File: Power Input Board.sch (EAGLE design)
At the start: 14 parts, among them Q1 SPB80P06P

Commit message: reconstructing
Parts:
- added J1, J2: (no value), SparkFun-Connectors:BANANA_CONN
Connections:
- net N$12 renamed +48V_GND
- removed net N$9: U$5.48V_GND
- removed net VCC: Q1.G
- new net +48V_RAW: J1.1, Q1.G
- new net 48V_GND: J2.1, R3.1, U$5.48V_GND
- net 3.3V: no longer R3.1
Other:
- note added: "48 VOLT CONNECTOR"
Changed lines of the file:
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@@
 <setting verticaltext="up"/>
 </settings>
-<grid distance="1" unitdist="mm" unit="mm" style="lines" multiple="1" display="no" altdistance="0.01" altunitdist="inch" altunit="inch"/>
+<grid distance="0.1" unitdist="inch" unit="inch" style="lines" multiple="1" display="no" altdistance="0.01" altunitdist="inch" altunit="inch"/>
 <layers>
 <layer number="1" name="Top" color="4" fill="1" visible="no" active="no"/>
@@
 <attribute name="SPICEPREFIX" value="R"/>
 </part>
-<part name="GND2" library="SparkFun-PowerSymbols" library_urn="urn:adsk.eagle:library:530" deviceset="GND2" device=""/>
-<part name="+48V" library="audio amplifier example" library_urn="urn:adsk.eagle:library:970892" deviceset="VCC" device="" value="48V"/>
 <part name="Q1" library="transistor-fet" library_urn="urn:adsk.eagle:library:396" deviceset="SPB80P06P" device="" package3d_urn="urn:adsk.eagle:package:28539/2"/>
 <part name="U$2" library="board_outlines" deviceset="BOARD" device="PDB"/>
@@
 <part name="U$5" library="PDB_TO_BRICKS" deviceset="BRICK_TO_POWER_DIST_WHOLE" device=""/>
 <part name="U$6" library="PDB_TO_BRICKS" deviceset="BRICK_TO_POWER_DIST_WHOLE" device=""/>
+<part name="J1" library="SparkFun-Connectors" deviceset="BANANA_CONN" device=""/>
+<part name="J2" library="SparkFun-Connectors" deviceset="BANANA_CONN" device=""/>
 </parts>
 <sheets>
 <sheet>
 <plain>
+<text x="30.48" y="106.68" size="2.54" layer="91">48 VOLT CONNECTOR</text>
 </plain>
 <instances>
@@
 <attribute name="NAME" x="145.796" y="195.58" size="1.778" layer="95" font="vector" rot="R90" align="bottom-center"/>
 <attribute name="VALUE" x="148.844" y="195.58" size="1.778" layer="96" font="vector" rot="R90" align="top-center"/>
-</instance>
-<instance part="GND2" gate="G$1" x="147.32" y="182.88">
-<attribute name="VALUE" x="147.32" y="181.102" size="1.778" layer="96" align="top-center"/>
-</instance>
-<instance part="+48V" gate="VCC" x="142.24" y="223.52">
-<attribute name="VALUE" x="140.716" y="224.536" size="1.27" layer="96"/>
 </instance>
 <instance part="Q1" gate="G$1" x="144.78" y="213.36">
@@
 <instance part="U$5" gate="G$1" x="297.18" y="147.32"/>
 <instance part="U$6" gate="G$1" x="297.18" y="119.38"/>
+<instance part="J1" gate="G$1" x="50.8" y="96.52"/>
+<instance part="J2" gate="G$1" x="50.8" y="91.44"/>
 </instances>
 <busses>
@@
 <wire x1="73.66" y1="180.34" x2="58.42" y2="180.34" width="0.1524" layer="91"/>
 </segment>
-<segment>
-<pinref part="GND2" gate="G$1" pin="3.3V"/>
-<wire x1="147.32" y1="185.42" x2="147.32" y2="190.5" width="0.1524" layer="91"/>
-<pinref part="R3" gate="G$1" pin="1"/>
-</segment>
 </net>
 <net name="N$3" class="0">
@@
 </segment>
 </net>
-<net name="VCC" class="0">
-<segment>
-<pinref part="Q1" gate="G$1" pin="G"/>
-<pinref part="+48V" gate="VCC" pin="VCC"/>
-<wire x1="142.24" y1="215.9" x2="142.24" y2="220.98" width="0.1524" layer="91"/>
-</segment>
-</net>
 <net name="+12V_1" class="0">
 <segment>
@@
 </segment>
 </net>
-<net name="N$9" class="0">
+<net name="N$10" class="0">
+<segment>
+<pinref part="U$5" gate="G$1" pin="D_GND"/>
+<wire x1="325.12" y1="149.86" x2="337.82" y2="149.86" width="0.1524" layer="91"/>
+</segment>
+</net>
+<net name="+48V_GND" class="0">
+<segment>
+<pinref part="U$6" gate="G$1" pin="48V_GND"/>
+<wire x1="325.12" y1="129.54" x2="337.82" y2="129.54" width="0.1524" layer="91"/>
+<label x="335.28" y="129.54" size="1.778" layer="95"/>
+</segment>
+</net>
+<net name="N$13" class="0">
+<segment>
+<pinref part="U$6" gate="G$1" pin="D_GND"/>
+<wire x1="325.12" y1="121.92" x2="337.82" y2="121.92" width="0.1524" layer="91"/>
+</segment>
+</net>
+<net name="48V_GND" class="0">
+<segment>
+<pinref part="J2" gate="G$1" pin="1"/>
+<wire x1="48.26" y1="91.44" x2="38.1" y2="91.44" width="0.1524" layer="91"/>
+<label x="38.1" y="91.44" size="1.778" layer="95"/>
+</segment>
+<segment>
+<wire x1="147.32" y1="185.42" x2="147.32" y2="190.5" width="0.1524" layer="91"/>
+<pinref part="R3" gate="G$1" pin="1"/>
+<wire x1="147.32" y1="185.42" x2="147.32" y2="180.34" width="0.1524" layer="91"/>
+<wire x1="147.32" y1="180.34" x2="152.4" y2="180.34" width="0.1524" layer="91"/>
+<label x="149.86" y="180.34" size="1.778" layer="95"/>
+</segment>
 <segment>
 <pinref part="U$5" gate="G$1" pin="48V_GND"/>
 <wire x1="325.12" y1="157.48" x2="337.82" y2="157.48" width="0.1524" layer="91"/>
-</segment>
-</net>
-<net name="N$10" class="0">
-<segment>
-<pinref part="U$5" gate="G$1" pin="D_GND"/>
-<wire x1="325.12" y1="149.86" x2="337.82" y2="149.86" width="0.1524" layer="91"/>
-</segment>
-</net>
-<net name="N$12" class="0">
-<segment>
-<pinref part="U$6" gate="G$1" pin="48V_GND"/>
-<wire x1="325.12" y1="129.54" x2="337.82" y2="129.54" width="0.1524" layer="91"/>
-</segment>
-</net>
-<net name="N$13" class="0">
-<segment>
-<pinref part="U$6" gate="G$1" pin="D_GND"/>
-<wire x1="325.12" y1="121.92" x2="337.82" y2="121.92" width="0.1524" layer="91"/>
-</segment>
-</net>
+<label x="335.28" y="157.48" size="1.778" layer="95"/>
+</segment>
+</net>
+<net name="+48V_RAW" class="0">
+<segment>
+<pinref part="J1" gate="G$1" pin="1"/>
+<wire x1="48.26" y1="96.52" x2="38.1" y2="96.52" width="0.1524" layer="91"/>
+<label x="38.1" y="96.52" size="1.778" layer="95"/>
+</segment>
+<segment>
+<pinref part="Q1" gate="G$1" pin="G"/>
+<wire x1="142.24" y1="215.9" x2="142.24" y2="220.98" width="0.1524" layer="91"/>
+<wire x1="142.24" y1="220.98" x2="142.24" y2="223.52" width="0.1524" layer="91"/>
+<wire x1="142.24" y1="223.52" x2="132.08" y2="223.52" width="0.1524" layer="91"/>
+<label x="132.08" y="223.52" size="1.778" layer="95"/>
+</segment>
+</net>

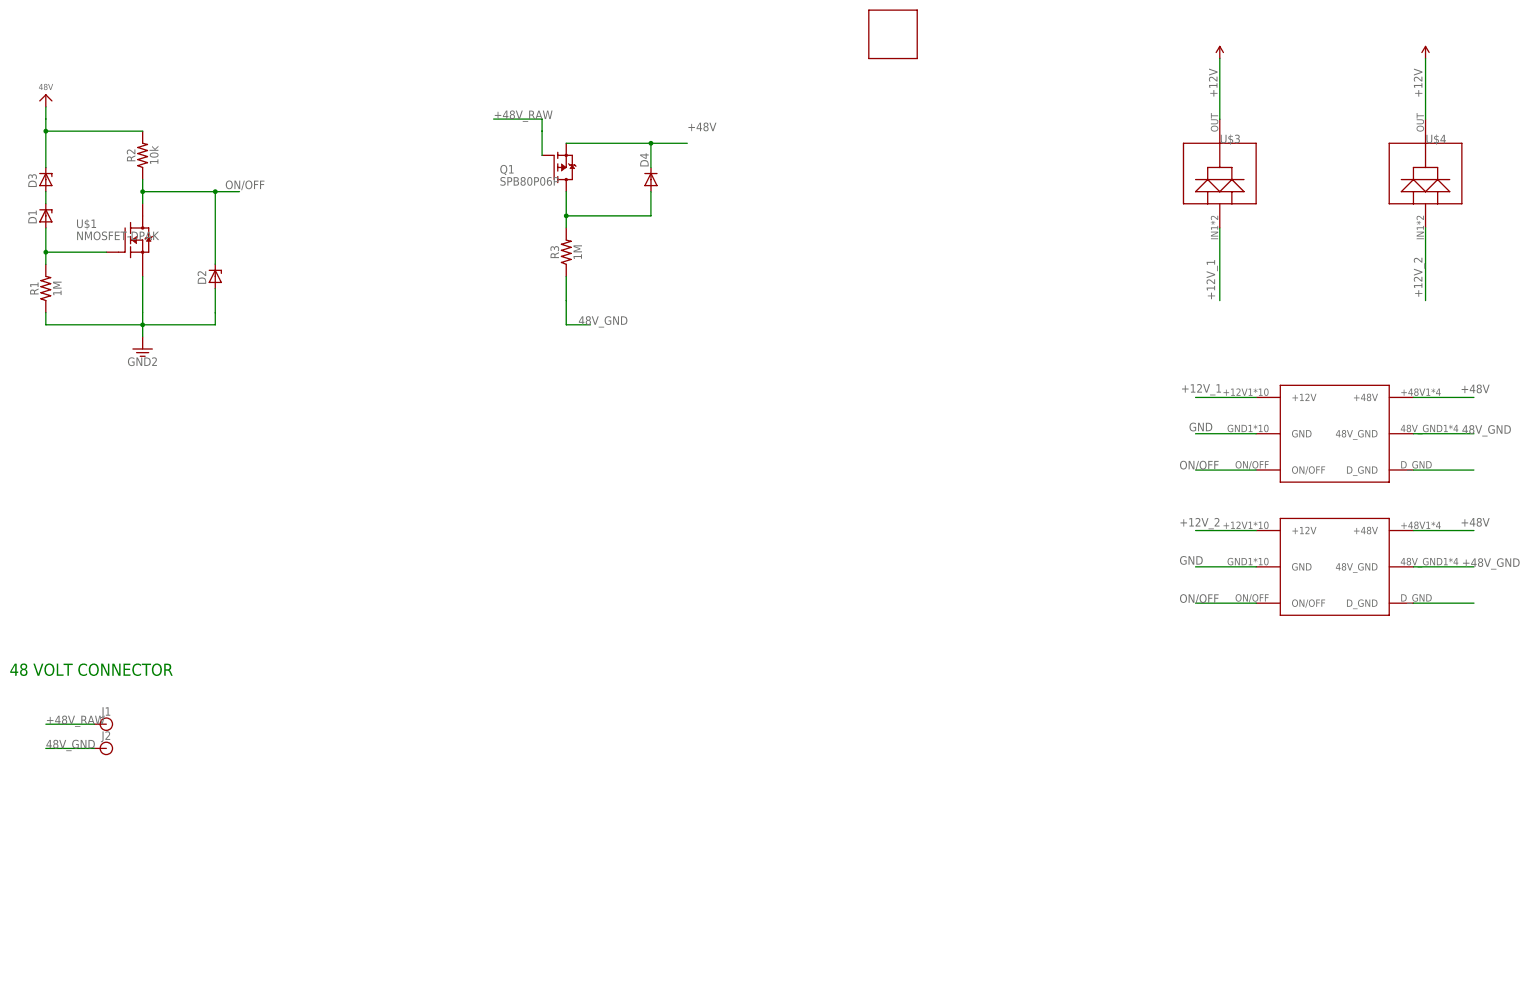
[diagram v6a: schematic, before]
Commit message: added connectors
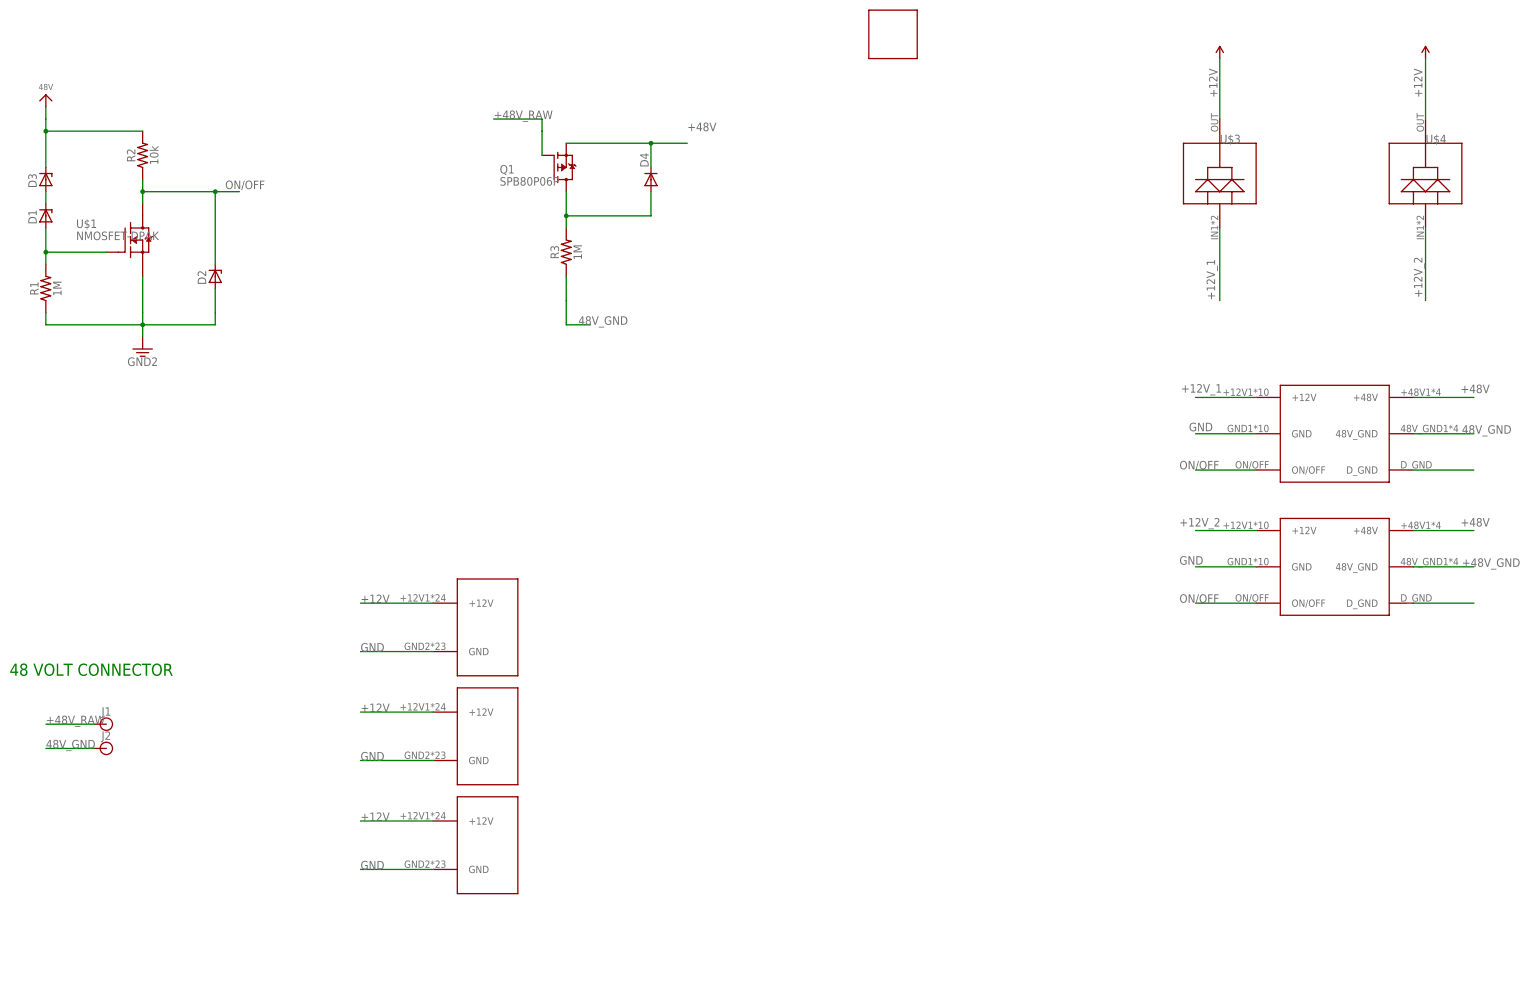
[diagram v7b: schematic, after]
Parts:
- added U$7, U$8, U$9: PDB_PCB_CONNEC, PDB_PCB_connectors:PDB_PCB_CONNEC
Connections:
- net +12V: now also U$7.+12V, U$8.+12V, U$9.+12V
- net GND: now also U$7.GND, U$8.GND, U$9.GND
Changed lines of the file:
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@@
 <?xml version="1.0" encoding="utf-8"?>
 <!DOCTYPE eagle SYSTEM "eagle.dtd">
-<eagle version="9.1.3">
+<eagle version="9.2.0">
 <drawing>
 <settings>
@@
 <part name="J1" library="SparkFun-Connectors" deviceset="BANANA_CONN" device=""/>
 <part name="J2" library="SparkFun-Connectors" deviceset="BANANA_CONN" device=""/>
+<part name="U$7" library="PDB_PCB_connectors" deviceset="PDB_PCB_CONNEC" device=""/>
+<part name="U$8" library="PDB_PCB_connectors" deviceset="PDB_PCB_CONNEC" device=""/>
+<part name="U$9" library="PDB_PCB_connectors" deviceset="PDB_PCB_CONNEC" device=""/>
 </parts>
 <sheets>
@@
 </instance>
 <instance part="U$2" gate="G$1" x="215.9" y="241.3"/>
-<instance part="U$3" gate="G$1" x="284.48" y="213.36"/>
-<instance part="U$4" gate="G$1" x="327.66" y="213.36"/>
-<instance part="SUPPLY1" gate="G$1" x="284.48" y="236.22"/>
-<instance part="SUPPLY2" gate="G$1" x="327.66" y="236.22"/>
+<instance part="U$3" gate="G$1" x="284.48" y="213.36">
+<attribute name="NAME" x="284.48" y="218.44" size="1.778" layer="95"/>
+</instance>
+<instance part="U$4" gate="G$1" x="327.66" y="213.36">
+<attribute name="NAME" x="327.66" y="218.44" size="1.778" layer="95"/>
+</instance>
+<instance part="SUPPLY1" gate="G$1" x="284.48" y="236.22">
+<attribute name="VALUE" x="284.48" y="239.014" size="1.778" layer="96" align="bottom-center"/>
+</instance>
+<instance part="SUPPLY2" gate="G$1" x="327.66" y="236.22">
+<attribute name="VALUE" x="327.66" y="239.014" size="1.778" layer="96" align="bottom-center"/>
+</instance>
 <instance part="U$5" gate="G$1" x="297.18" y="147.32"/>
 <instance part="U$6" gate="G$1" x="297.18" y="119.38"/>
-<instance part="J1" gate="G$1" x="50.8" y="96.52"/>
-<instance part="J2" gate="G$1" x="50.8" y="91.44"/>
+<instance part="J1" gate="G$1" x="50.8" y="96.52">
+<attribute name="NAME" x="49.784" y="98.298" size="1.778" layer="95" font="vector"/>
+<attribute name="VALUE" x="49.784" y="93.472" size="1.778" layer="96" font="vector"/>
+</instance>
+<instance part="J2" gate="G$1" x="50.8" y="91.44">
+<attribute name="NAME" x="49.784" y="93.218" size="1.778" layer="95" font="vector"/>
+<attribute name="VALUE" x="49.784" y="88.392" size="1.778" layer="96" font="vector"/>
+</instance>
+<instance part="U$7" gate="G$1" x="124.46" y="106.68"/>
+<instance part="U$8" gate="G$1" x="124.46" y="83.82"/>
+<instance part="U$9" gate="G$1" x="124.46" y="60.96"/>
 </instances>
 <busses>
@@
 <label x="327" y="228" size="1.778" layer="95" rot="R90"/>
 </segment>
+<segment>
+<pinref part="U$7" gate="G$1" pin="+12V"/>
+<wire x1="119.38" y1="121.92" x2="104.14" y2="121.92" width="0.1524" layer="91"/>
+<label x="104.14" y="121.92" size="1.778" layer="95"/>
+</segment>
+<segment>
+<pinref part="U$8" gate="G$1" pin="+12V"/>
+<wire x1="119.38" y1="99.06" x2="104.14" y2="99.06" width="0.1524" layer="91"/>
+<label x="104.14" y="99.06" size="1.778" layer="95"/>
+</segment>
+<segment>
+<pinref part="U$9" gate="G$1" pin="+12V"/>
+<wire x1="119.38" y1="76.2" x2="104.14" y2="76.2" width="0.1524" layer="91"/>
+<label x="104.14" y="76.2" size="1.778" layer="95"/>
+</segment>
 </net>
 <net name="GND" class="0">
@@
 <label x="276" y="130" size="1.778" layer="95"/>
 </segment>
-</net>
+<segment>
+<pinref part="U$7" gate="G$1" pin="GND"/>
+<wire x1="119.38" y1="111.76" x2="104.14" y2="111.76" width="0.1524" layer="91"/>
+<label x="104.14" y="111.76" size="1.778" layer="95"/>
+</segment>
+<segment>
+<pinref part="U$8" gate="G$1" pin="GND"/>
+<wire x1="119.38" y1="88.9" x2="104.14" y2="88.9" width="0.1524" layer="91"/>
+<label x="104.14" y="88.9" size="1.778" layer="95"/>
+</segment>
+<segment>
+<pinref part="U$9" gate="G$1" pin="GND"/>
+<wire x1="119.38" y1="66.04" x2="104.14" y2="66.04" width="0.1524" layer="91"/>
+<label x="104.14" y="66.04" size="1.778" layer="95"/>
+</segment>
+</net>

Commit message: routed roughly
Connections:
- removed net +48V_GND: U$6.48V_GND
- net 48V_GND: now also U$6.48V_GND
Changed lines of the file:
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@@
 <attribute name="VALUE" x="49.784" y="88.392" size="1.778" layer="96" font="vector"/>
 </instance>
-<instance part="U$7" gate="G$1" x="124.46" y="106.68"/>
-<instance part="U$8" gate="G$1" x="124.46" y="83.82"/>
-<instance part="U$9" gate="G$1" x="124.46" y="60.96"/>
+<instance part="U$7" gate="G$1" x="99.06" y="86.36"/>
+<instance part="U$8" gate="G$1" x="99.06" y="63.5"/>
+<instance part="U$9" gate="G$1" x="99.06" y="40.64"/>
 </instances>
 <busses>
@@
 <wire x1="165.1" y1="213.36" x2="165.1" y2="218.44" width="0.1524" layer="91"/>
 <wire x1="165.1" y1="218.44" x2="172.72" y2="218.44" width="0.1524" layer="91"/>
-<label x="172.72" y="220.98" size="1.778" layer="95"/>
+<label x="170.18" y="218.44" size="1.778" layer="95"/>
 <pinref part="Q1" gate="G$1" pin="S"/>
 <wire x1="147.32" y1="218.44" x2="165.1" y2="218.44" width="0.1524" layer="91"/>
@@
 <segment>
 <pinref part="U$7" gate="G$1" pin="+12V"/>
-<wire x1="119.38" y1="121.92" x2="104.14" y2="121.92" width="0.1524" layer="91"/>
-<label x="104.14" y="121.92" size="1.778" layer="95"/>
+<wire x1="93.98" y1="101.6" x2="78.74" y2="101.6" width="0.1524" layer="91"/>
+<label x="78.74" y="101.6" size="1.778" layer="95"/>
 </segment>
 <segment>
 <pinref part="U$8" gate="G$1" pin="+12V"/>
-<wire x1="119.38" y1="99.06" x2="104.14" y2="99.06" width="0.1524" layer="91"/>
-<label x="104.14" y="99.06" size="1.778" layer="95"/>
+<wire x1="93.98" y1="78.74" x2="78.74" y2="78.74" width="0.1524" layer="91"/>
+<label x="78.74" y="78.74" size="1.778" layer="95"/>
 </segment>
 <segment>
 <pinref part="U$9" gate="G$1" pin="+12V"/>
-<wire x1="119.38" y1="76.2" x2="104.14" y2="76.2" width="0.1524" layer="91"/>
-<label x="104.14" y="76.2" size="1.778" layer="95"/>
+<wire x1="93.98" y1="55.88" x2="78.74" y2="55.88" width="0.1524" layer="91"/>
+<label x="78.74" y="55.88" size="1.778" layer="95"/>
 </segment>
 </net>
@@
 <segment>
 <pinref part="U$7" gate="G$1" pin="GND"/>
-<wire x1="119.38" y1="111.76" x2="104.14" y2="111.76" width="0.1524" layer="91"/>
-<label x="104.14" y="111.76" size="1.778" layer="95"/>
+<wire x1="93.98" y1="91.44" x2="78.74" y2="91.44" width="0.1524" layer="91"/>
+<label x="78.74" y="91.44" size="1.778" layer="95"/>
 </segment>
 <segment>
 <pinref part="U$8" gate="G$1" pin="GND"/>
-<wire x1="119.38" y1="88.9" x2="104.14" y2="88.9" width="0.1524" layer="91"/>
-<label x="104.14" y="88.9" size="1.778" layer="95"/>
+<wire x1="93.98" y1="68.58" x2="78.74" y2="68.58" width="0.1524" layer="91"/>
+<label x="78.74" y="68.58" size="1.778" layer="95"/>
 </segment>
 <segment>
 <pinref part="U$9" gate="G$1" pin="GND"/>
-<wire x1="119.38" y1="66.04" x2="104.14" y2="66.04" width="0.1524" layer="91"/>
-<label x="104.14" y="66.04" size="1.778" layer="95"/>
+<wire x1="93.98" y1="45.72" x2="78.74" y2="45.72" width="0.1524" layer="91"/>
+<label x="78.74" y="45.72" size="1.778" layer="95"/>
 </segment>
 </net>
@@
 <pinref part="U$5" gate="G$1" pin="D_GND"/>
 <wire x1="325.12" y1="149.86" x2="337.82" y2="149.86" width="0.1524" layer="91"/>
-</segment>
-</net>
-<net name="+48V_GND" class="0">
-<segment>
-<pinref part="U$6" gate="G$1" pin="48V_GND"/>
-<wire x1="325.12" y1="129.54" x2="337.82" y2="129.54" width="0.1524" layer="91"/>
-<label x="335.28" y="129.54" size="1.778" layer="95"/>
 </segment>
 </net>
@@
 <label x="335.28" y="157.48" size="1.778" layer="95"/>
 </segment>
-</net>
+<segment>
+<pinref part="U$6" gate="G$1" pin="48V_GND"/>
+<wire x1="325.12" y1="129.54" x2="337.82" y2="129.54" width="0.1524" layer="91"/>
+<label x="335.28" y="129.54" size="1.778" layer="95"/>
+</segment>
+</net>
